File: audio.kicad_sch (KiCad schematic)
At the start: 0 parts

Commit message: Added custom U78 to the audio sub sheet. Ready for audio schematic capture of custom audio interface
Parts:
- added U78: ALC269Q-VB6-CG, Package_DFN_QFN:QFN-48-1EP_7x7mm_P0.5mm_EP5.15x5.15mm, symbol Custom_Audio:ALC269Q-VB6-CG
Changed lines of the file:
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@@
 	(generator "eeschema")
 	(generator_version "10.0")
-	(paper "A3")
+	(paper "A2")
+	(bus_entry
+		(at 154.94 104.14)
+		(size 2.54 2.54)
+		(stroke
+			(width 0)
+			(type default)
+		)
+	)
+	(symbol
+		(lib_id "Custom_Audio:ALC269Q-VB6-CG")
+		(at 398.78 280.67 0)
+		(unit 1)
+		(body_style 1)
+		(exclude_from_sim no)
+		(in_bom yes)
+		(on_board yes)
+		(in_pos_files yes)
+		(dnp no)
+		(property "Reference" "U78"
+			(at 295.402 175.26 0)
+			(show_name no)
+			(do_not_autoplace no)
+			(effects
+				(font
+					(size 1.27 1.27)
+				)
+				(justify left)
+			)
+		)
+		(property "Value" "ALC269Q-VB6-CG"
+			(at 288.798 177.292 0)
+			(show_name no)
+			(do_not_autoplace no)
+			(effects
+				(font
+					(size 1.27 1.27)
+				)
+				(justify left)
+			)
+		)
+		(property "Footprint" "Package_DFN_QFN:QFN-48-1EP_7x7mm_P0.5mm_EP5.15x5.15mm"
+			(at 398.78 280.67 0)
+			(hide yes)
+			(show_name no)
+			(do_not_autoplace no)
+			(effects
+				(font
+					(size 1.27 1.27)
+				)
+			)
+		)
+		(property "Datasheet" ""
+			(at 398.78 280.67 0)
+			(hide yes)
+			(show_name no)
+			(do_not_autoplace no)
+			(effects
+				(font
+					(size 1.27 1.27)
+				)
+			)
+		)
+		(property "Description" ""
+			(at 398.78 280.67 0)
+			(hide yes)
+			(show_name no)
+			(do_not_autoplace no)
+			(effects
+				(font
+					(size 1.27 1.27)
+				)
+			)
+		)
+		(pin "33"
+		)
+		(pin "34"
+		)
+		(pin "39"
+		)
+		(pin "24"
+		)
+		(pin "23"
+		)
+		(pin "36"
+		)
+		(pin "35"
+		)
+		(pin "19"
+		)
+		(pin "20"
+		)
+		(pin "22"
+		)
+		(pin "21"
+		)
+		(pin "37"
+		)
+		(pin "38"
+		)
+		(pin "42"
+		)
+		(pin "40"
+		)
+		(pin "41"
+		)
+		(pin "48"
+		)
+		(pin "43"
+		)
+		(pin "44"
+		)
+		(pin "49"
+		)
+		(pin "45"
+		)
+		(pin "46"
+		)
+		(pin "47"
+		)
+		(pin "29"
+		)
+		(pin "25"
+		)
+		(pin "28"
+		)
+		(pin "30"
+		)
+		(pin "32"
+		)
+		(pin "31"
+		)
+		(pin "27"
+		)
+		(pin "26"
+		)
+		(pin "2"
+		)
+		(pin "3"
+		)
+		(pin "18"
+		)
+		(pin "7"
+		)
+		(pin "10"
+		)
+		(pin "17"
+		)
+		(pin "1"
+		)
+		(pin "5"
+		)
+		(pin "4"
+		)
+		(pin "6"
+		)
+		(pin "9"
+		)
+		(pin "11"
+		)
+		(pin "16"
+		)
+		(pin "13"
+		)
+		(pin "12"
+		)
+		(pin "8"
+		)
+		(pin "14"
+		)
+		(pin "15"
+		)
+		(instances
+			(project "Carrier_Board"
+				(path "/e768274e-12f3-4f83-96f6-abb7638e0bc1/82ad3407-57b9-41ac-a23a-ddb5c849f2e7"
+					(reference "U78")
+					(unit 1)
+				)
+			)
+		)
+	)
 )

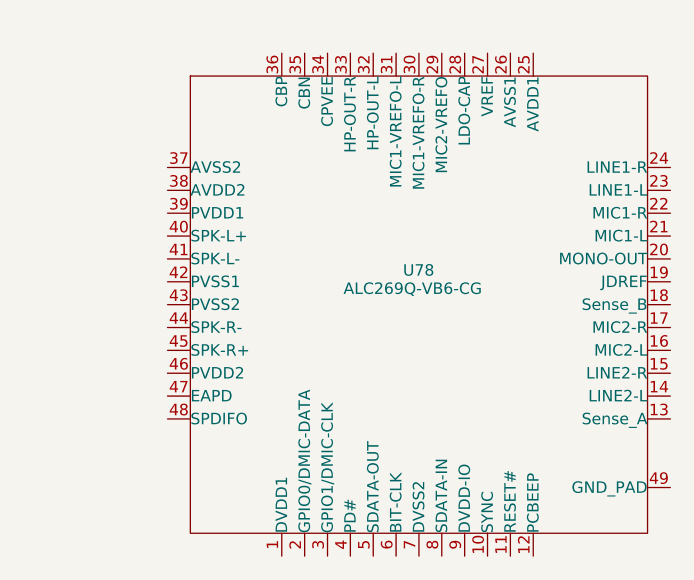
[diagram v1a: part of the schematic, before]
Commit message: Updated umpopul;ated audio pins in sub audio sheet
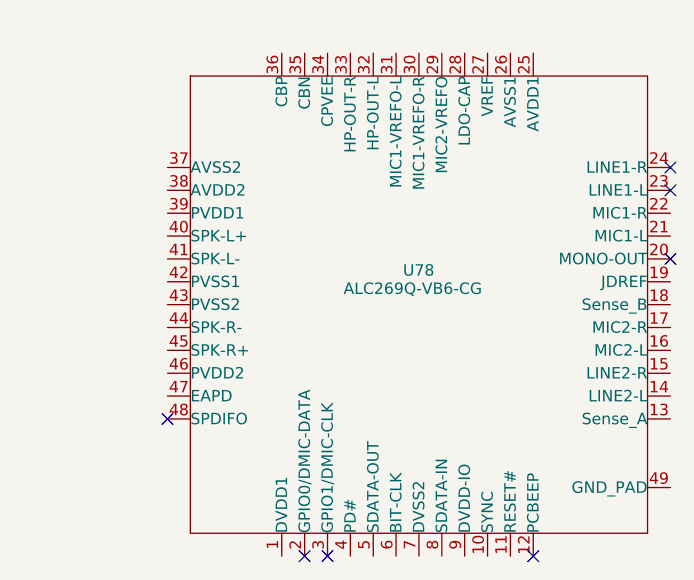
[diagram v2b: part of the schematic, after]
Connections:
- no-connect marks 0 -> 7
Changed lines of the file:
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@@
 	(generator_version "10.0")
 	(paper "A2")
+	(no_connect
+		(at 325.12 166.37)
+	)
+	(no_connect
+		(at 309.88 207.01)
+	)
+	(no_connect
+		(at 325.12 163.83)
+	)
+	(no_connect
+		(at 284.48 207.01)
+	)
+	(no_connect
+		(at 287.02 207.01)
+	)
+	(no_connect
+		(at 325.12 173.99)
+	)
+	(no_connect
+		(at 269.24 191.77)
+	)
 	(bus_entry
 		(at 154.94 104.14)

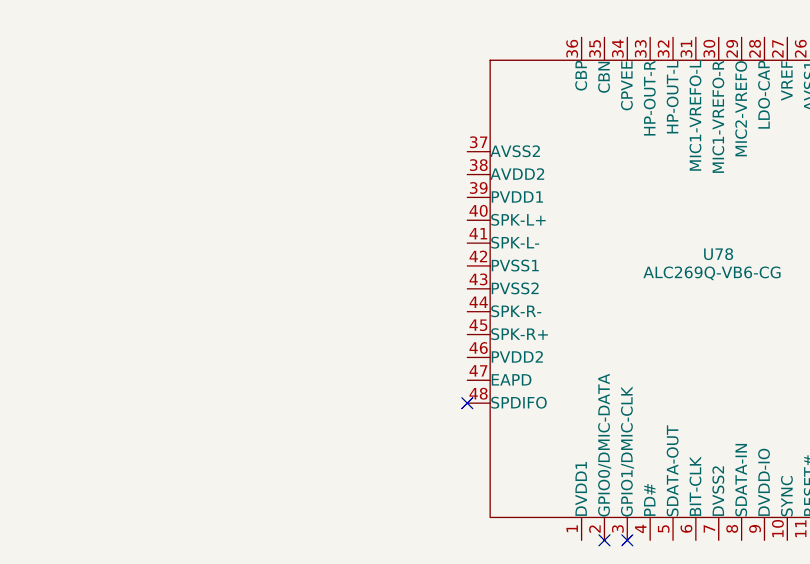
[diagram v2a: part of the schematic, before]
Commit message: Started the audio circuit and moved all parts onto the board
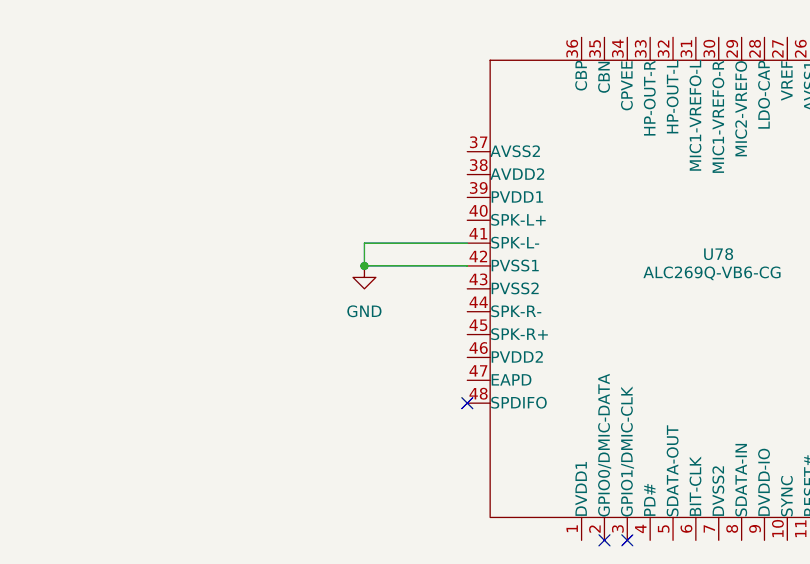
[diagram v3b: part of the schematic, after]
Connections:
- net GND: now reaches U78.41 (SPK-L-)
- net GND: now also U78.42 (PVSS1)
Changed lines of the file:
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@@
 	(generator_version "10.0")
 	(paper "A2")
+	(junction
+		(at 257.81 176.53)
+		(diameter 0)
+		(color 0 0 0 0)
+	)
 	(no_connect
 		(at 325.12 166.37)
@@
 		(at 154.94 104.14)
 		(size 2.54 2.54)
+		(stroke
+			(width 0)
+			(type default)
+		)
+	)
+	(wire
+		(pts
+			(xy 269.24 173.99) (xy 257.81 173.99)
+		)
+		(stroke
+			(width 0)
+			(type default)
+		)
+	)
+	(wire
+		(pts
+			(xy 257.81 173.99) (xy 257.81 176.53)
+		)
+		(stroke
+			(width 0)
+			(type default)
+		)
+	)
+	(wire
+		(pts
+			(xy 257.81 176.53) (xy 269.24 176.53)
+		)
 		(stroke
 			(width 0)
@@
 					(unit 1)
 				)
+			)
+		)
+	)
+	(symbol
+		(lib_id "power:GND")
+		(at 257.81 176.53 0)
+		(unit 1)
+		(body_style 1)
+		(exclude_from_sim no)
+		(in_bom yes)
+		(on_board yes)
+		(in_pos_files yes)
+		(dnp no)
+		(fields_autoplaced yes)
+		(property "Reference" "#PWR0205"
+			(at 257.81 182.88 0)
+			(hide yes)
+			(show_name no)
+			(do_not_autoplace no)
+			(effects
+				(font
+					(size 1.27 1.27)
+				)
+			)
+		)
+		(property "Value" "GND"
+			(at 257.81 181.61 0)
+			(show_name no)
+			(do_not_autoplace no)
+			(effects
+				(font
+					(size 1.27 1.27)
+				)
+			)
+		)
+		(property "Footprint" ""
+			(at 257.81 176.53 0)
+			(hide yes)
+			(show_name no)
+			(do_not_autoplace no)
+			(effects
+				(font
+					(size 1.27 1.27)
+				)
+			)
+		)
+		(property "Datasheet" ""
+			(at 257.81 176.53 0)
+			(hide yes)
+			(show_name no)
+			(do_not_autoplace no)
+			(effects
+				(font
+					(size 1.27 1.27)
+				)
+			)
+		)
+		(property "Description" "Power symbol creates a global label with name \"GND\" , ground"
+			(at 257.81 176.53 0)
+			(hide yes)
+			(show_name no)
+			(do_not_autoplace no)
+			(effects
+				(font
+					(size 1.27 1.27)
+				)
+			)
+		)
+		(pin "1"
+		)
+		(instances
+			(project "Carrier_Board"
+				(path "/e768274e-12f3-4f83-96f6-abb7638e0bc1/82ad3407-57b9-41ac-a23a-ddb5c849f2e7"
+					(reference "#PWR0205")
+					(unit 1)
+				)

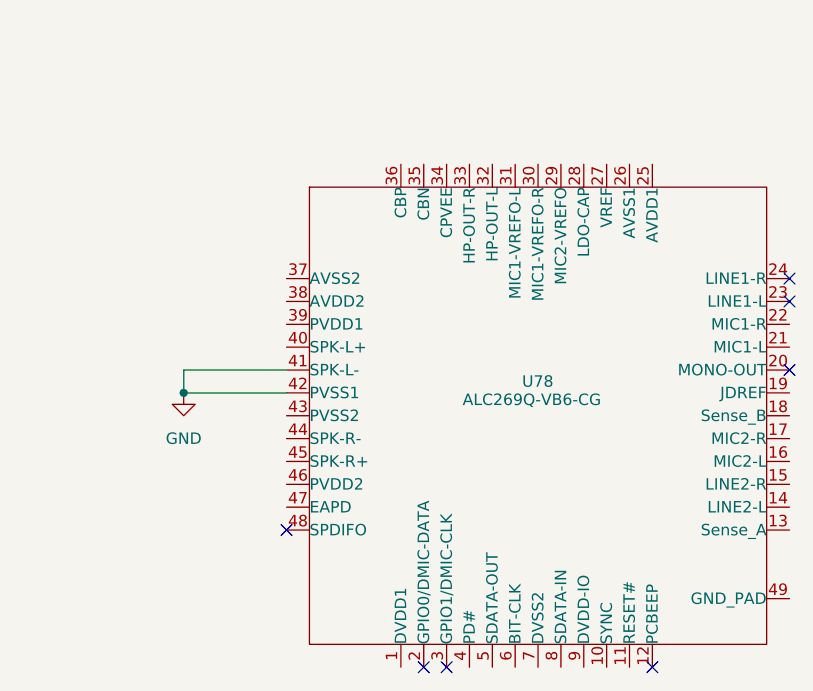
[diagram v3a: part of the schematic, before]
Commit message: Freed up some panda module labels for the wifi/bluetooth chip, and also organized the routes for the gpio connectors into blue layer 2 bundals... not fully connected yet
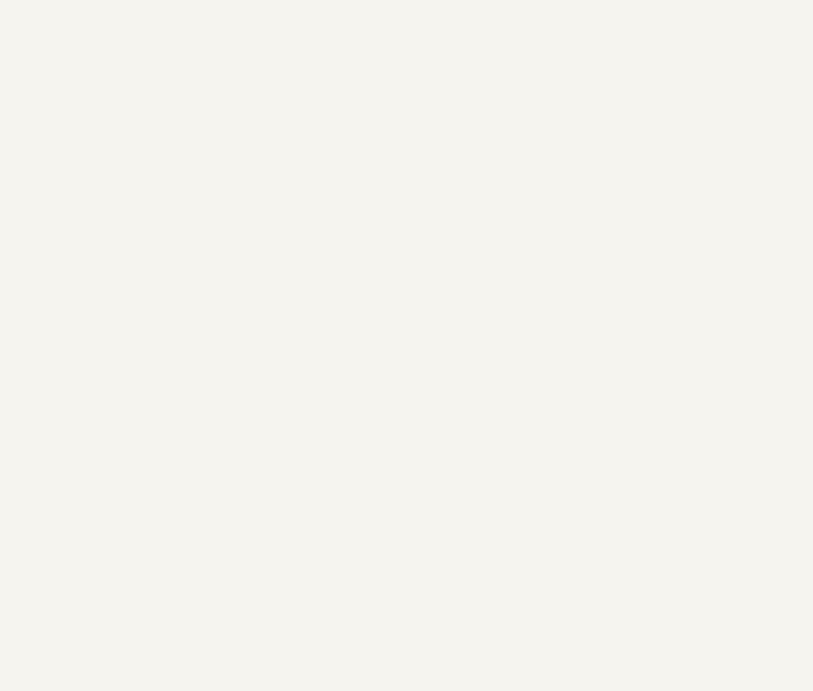
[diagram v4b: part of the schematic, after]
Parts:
- removed U78: ALC269Q-VB6-CG, Package_DFN_QFN:QFN-48-1EP_7x7mm_P0.5mm_EP5.15x5.15mm, symbol Custom_Audio:ALC269Q-VB6-CG
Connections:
- no-connect marks 7 -> 0

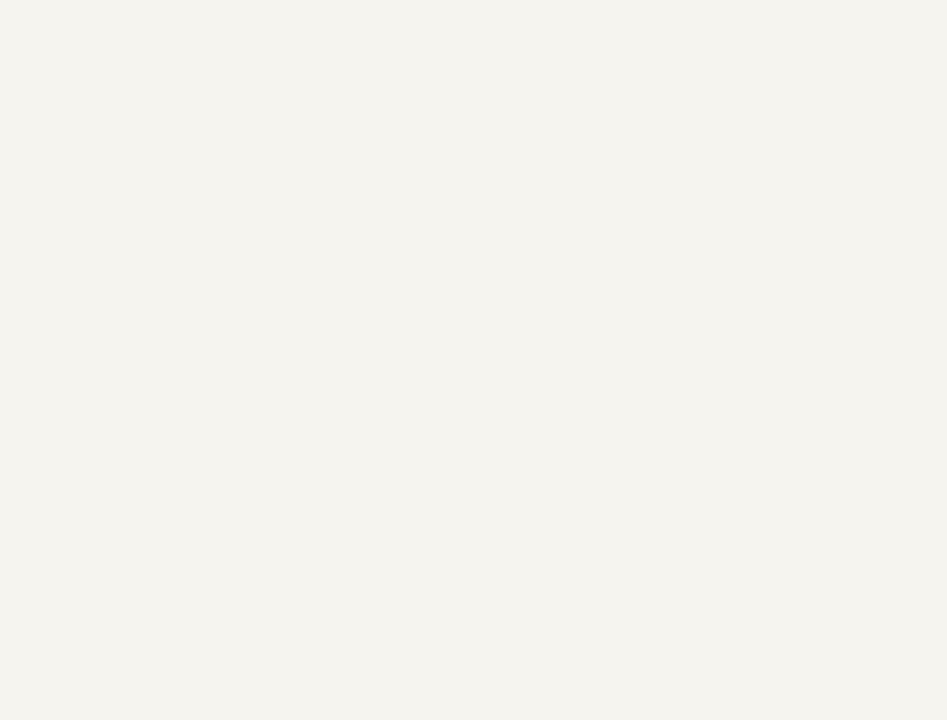
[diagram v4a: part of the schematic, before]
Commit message: Repaired the Audio and the wifiBT sheet relationship and recovered audio IC deletion
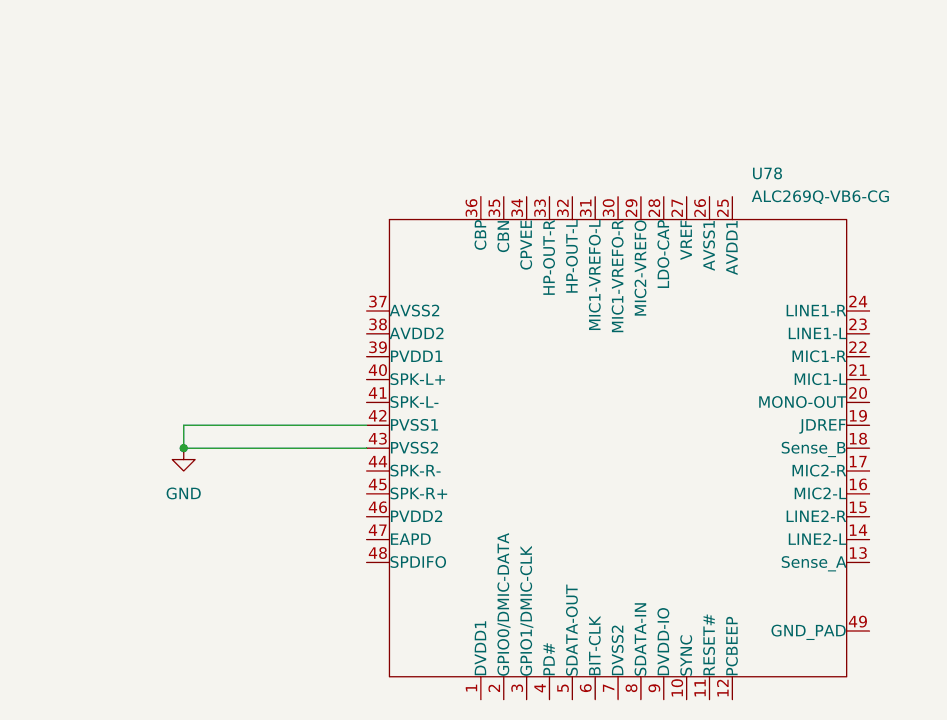
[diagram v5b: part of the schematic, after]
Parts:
- added U78: ALC269Q-VB6-CG, Package_DFN_QFN:QFN-48-1EP_7x7mm_P0.5mm_EP5.15x5.15mm, symbol Custom_Audio:ALC269Q-VB6-CG
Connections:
- new net GND: U78.42 (PVSS1), U78.43 (PVSS2)

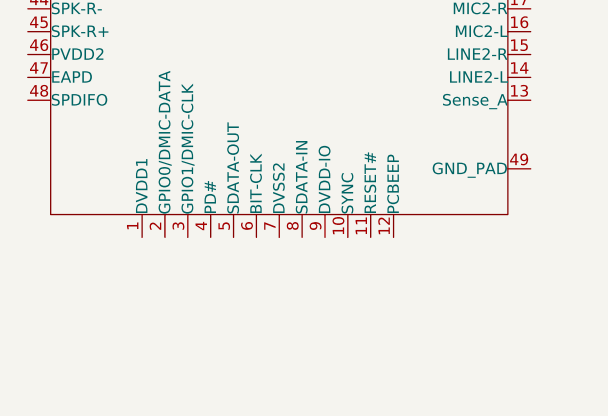
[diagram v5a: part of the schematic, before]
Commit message: Finished routing the GPIO and tested a route for the PCIE but i will need to add another layer. Trying to get all the sytems primed before i do the copper pours. Deviating from the course now. Wifi blue tooth sheet is set up and the audio sheet is ready for schematic capture
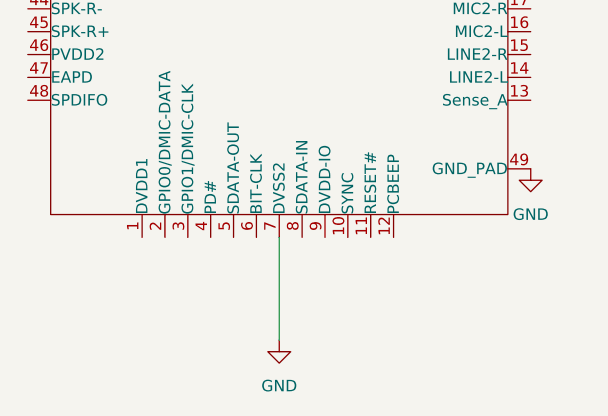
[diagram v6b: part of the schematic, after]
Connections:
- net GND: now also U78.49 (GND_PAD), U78.7 (DVSS2)
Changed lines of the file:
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@@
+	(wire
+		(pts
+			(xy 285.75 223.52) (xy 285.75 234.95)
+		)
+		(stroke
+			(width 0)
+			(type default)
+		)
+	)
 	(wire
 		(pts
@@
 			(width 0)
 			(type default)
+		)
+	)
+	(symbol
+		(lib_id "power:GND")
+		(at 285.75 234.95 0)
+		(unit 1)
+		(body_style 1)
+		(exclude_from_sim no)
+		(in_bom yes)
+		(on_board yes)
+		(in_pos_files yes)
+		(dnp no)
+		(fields_autoplaced yes)
+		(property "Reference" "#PWR0207"
+			(at 285.75 241.3 0)
+			(hide yes)
+			(show_name no)
+			(do_not_autoplace no)
+			(effects
+				(font
+					(size 1.27 1.27)
+				)
+			)
+		)
+		(property "Value" "GND"
+			(at 285.75 240.03 0)
+			(show_name no)
+			(do_not_autoplace no)
+			(effects
+				(font
+					(size 1.27 1.27)
+				)
+			)
+		)
+		(property "Footprint" ""
+			(at 285.75 234.95 0)
+			(hide yes)
+			(show_name no)
+			(do_not_autoplace no)
+			(effects
+				(font
+					(size 1.27 1.27)
+				)
+			)
+		)
+		(property "Datasheet" ""
+			(at 285.75 234.95 0)
+			(hide yes)
+			(show_name no)
+			(do_not_autoplace no)
+			(effects
+				(font
+					(size 1.27 1.27)
+				)
+			)
+		)
+		(property "Description" "Power symbol creates a global label with name \"GND\" , ground"
+			(at 285.75 234.95 0)
+			(hide yes)
+			(show_name no)
+			(do_not_autoplace no)
+			(effects
+				(font
+					(size 1.27 1.27)
+				)
+			)
+		)
+		(pin "1"
+		)
+		(instances
+			(project "Carrier_Board"
+				(path "/e768274e-12f3-4f83-96f6-abb7638e0bc1/82ad3407-57b9-41ac-a23a-ddb5c849f2e7"
+					(reference "#PWR0207")
+					(unit 1)
+				)
+			)
 		)
 	)
@@
 					(unit 1)
 				)
+			)
+		)
+	)
+	(symbol
+		(lib_id "power:GND")
+		(at 313.69 215.9 0)
+		(unit 1)
+		(body_style 1)
+		(exclude_from_sim no)
+		(in_bom yes)
+		(on_board yes)
+		(in_pos_files yes)
+		(dnp no)
+		(fields_autoplaced yes)
+		(property "Reference" "#PWR0206"
+			(at 313.69 222.25 0)
+			(hide yes)
+			(show_name no)
+			(do_not_autoplace no)
+			(effects
+				(font
+					(size 1.27 1.27)
+				)
+			)
+		)
+		(property "Value" "GND"
+			(at 313.69 220.98 0)
+			(show_name no)
+			(do_not_autoplace no)
+			(effects
+				(font
+					(size 1.27 1.27)
+				)
+			)
+		)
+		(property "Footprint" ""
+			(at 313.69 215.9 0)
+			(hide yes)
+			(show_name no)
+			(do_not_autoplace no)
+			(effects
+				(font
+					(size 1.27 1.27)
+				)
+			)
+		)
+		(property "Datasheet" ""
+			(at 313.69 215.9 0)
+			(hide yes)
+			(show_name no)
+			(do_not_autoplace no)
+			(effects
+				(font
+					(size 1.27 1.27)
+				)
+			)
+		)
+		(property "Description" "Power symbol creates a global label with name \"GND\" , ground"
+			(at 313.69 215.9 0)
+			(hide yes)
+			(show_name no)
+			(do_not_autoplace no)
+			(effects
+				(font
+					(size 1.27 1.27)
+				)
+			)
+		)
+		(pin "1"
+		)
+		(instances
+			(project "Carrier_Board"
+				(path "/e768274e-12f3-4f83-96f6-abb7638e0bc1/82ad3407-57b9-41ac-a23a-ddb5c849f2e7"
+					(reference "#PWR0206")
+					(unit 1)
+				)
